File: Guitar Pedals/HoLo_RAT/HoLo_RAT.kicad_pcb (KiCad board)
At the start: 2 copper layers, 68.6 x 97.8 mm, 35 parts, among them Q1 2n5458, U1 OP07

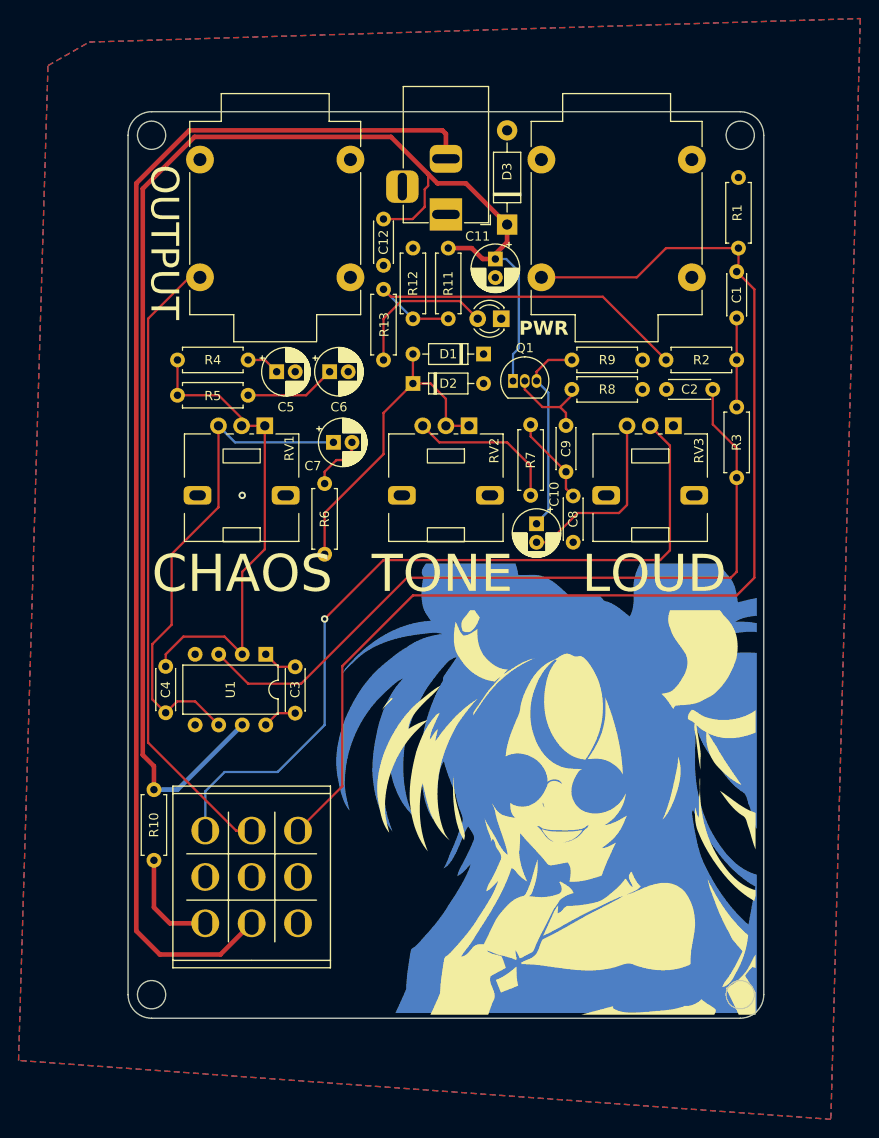
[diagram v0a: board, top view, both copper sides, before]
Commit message: [HoLo_RAT] Fixed TR pinout
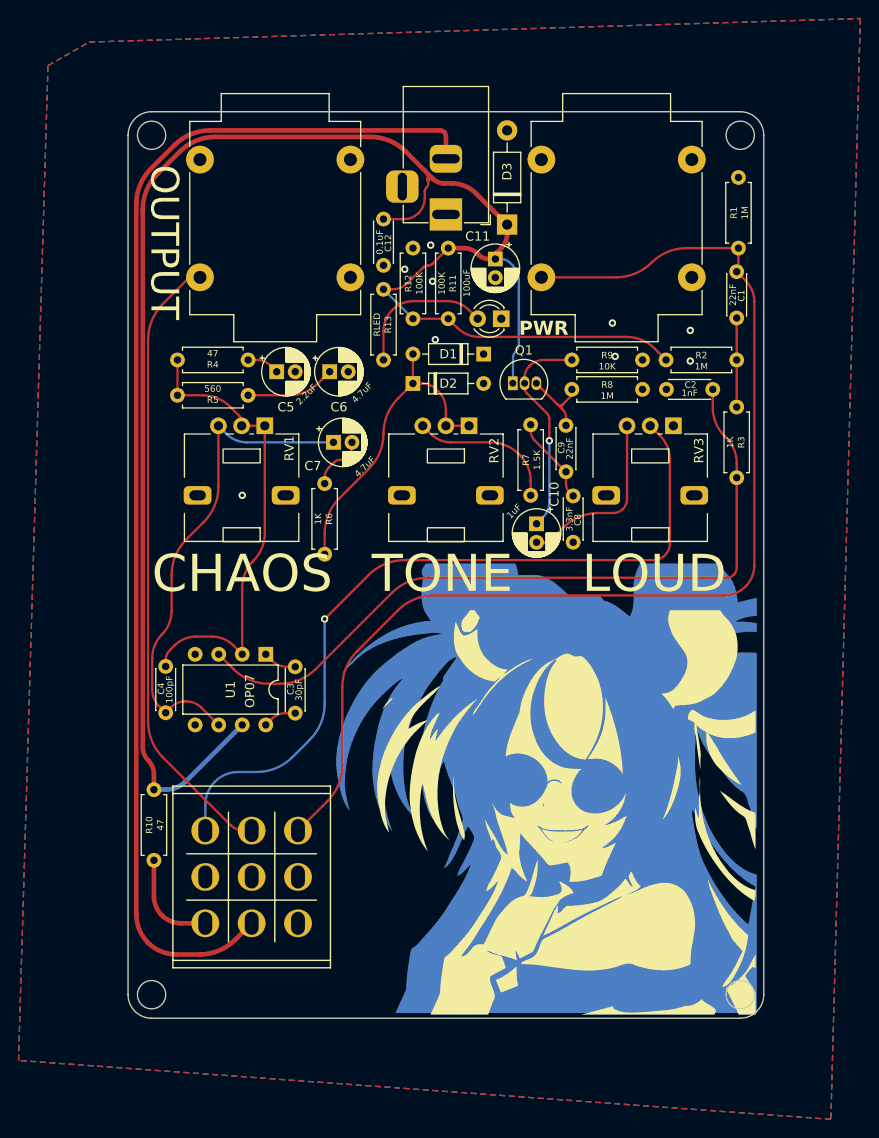
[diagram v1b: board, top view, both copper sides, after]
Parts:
- C1, C12, C2, C3, C4, C8, C9: footprint Capacitor_THT:C_Disc_D4.3mm_W1.9mm_P5.00mm -> Charlie_Lee_Rhee_Custom_Parts:C_Custom_Disc_D4.3mm_W1.9mm_P5.00mm
- Q1: value 2n5458 -> 2N5458; footprint Package_TO_SOT_THT:TO-92_Inline -> Package_TO_SOT_THT:TO-92L_Inline
- R1, R10, R11, R12, R2, R3, R4, R5, R6, R7, R8, R9: footprint Resistor_THT:R_Axial_DIN0207_L6.3mm_D2.5mm_P7.62mm_Horizontal -> Charlie_Lee_Rhee_Custom_Parts:R_Custom_Axial_DIN0207_L6.3mm_D2.5mm_P7.62mm_Horizontal
- R13: value 1K -> RLED; footprint Resistor_THT:R_Axial_DIN0207_L6.3mm_D2.5mm_P7.62mm_Horizontal -> Charlie_Lee_Rhee_Custom_Parts:R_Custom_Axial_DIN0207_L6.3mm_D2.5mm_P7.62mm_Horizontal
- moved Q1 0.25 mm to (170.2, 60.3)
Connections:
- Q1 pad 2: Net-(Q1-G) -> Net-(Q1-S)
- Q1 pad 3: Net-(Q1-S) -> Net-(Q1-G)
- R13 pad 1: 4.5V -> 9V
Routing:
- net 4.5V: track 41.9 -> 33.3 mm
- net 9V: track 156.9 -> 164.2 mm
- net DRY: track 127.1 -> 125.3 mm
- net Net-(C4-Pad1): track 54.9 -> 53.2 mm
- net Net-(Q1-S): track 21.8 -> 23.4 mm, vias 0 -> 1
- net WET: track 86.1 -> 84.7 mm
- net Net-(U1-+): track 82.9 -> 81.7 mm
- net VIN: track 134.1 -> 132.9 mm
- net Net-(U1--): track 51.9 -> 50.6 mm
- net Net-(Q1-G): track 10.2 -> 9.14 mm
- net Net-(D1-A): track 35.2 -> 34.2 mm
- net OUT: track 68.3 -> 67.6 mm
- net Net-(R7-Pad1): track 16.6 -> 16.1 mm
- net GND: vias 1 -> 9
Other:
- board text added: "&#39;"
